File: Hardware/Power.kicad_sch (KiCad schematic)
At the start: 12 parts

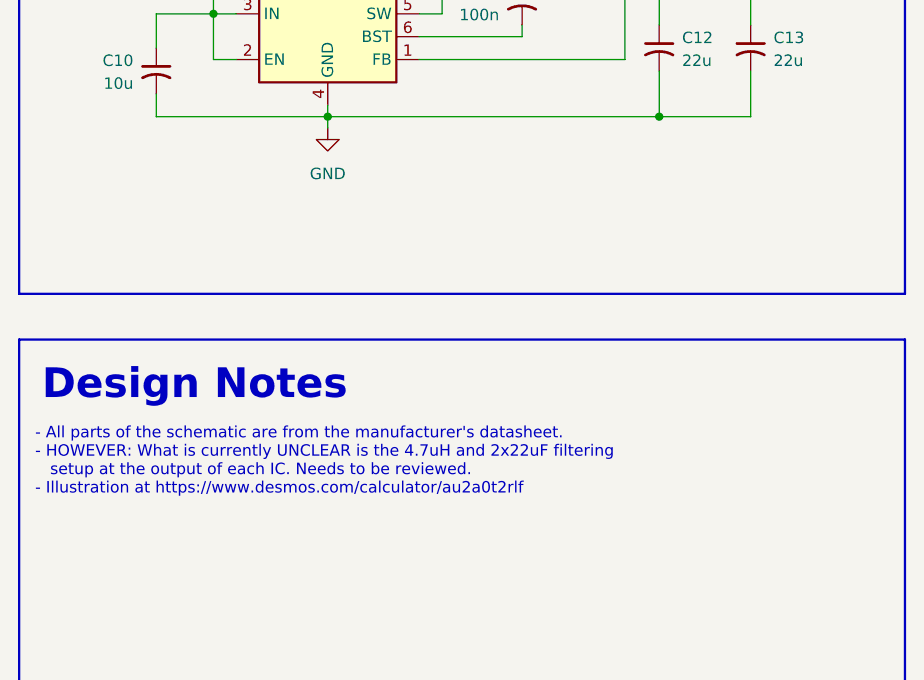
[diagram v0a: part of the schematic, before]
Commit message: Finished the ISOW1044 Schematic
- Ported over Kostadin's schematic

Co-authored-by: Kostadin Madjovski <155325994+bivein@users.noreply.github.com>
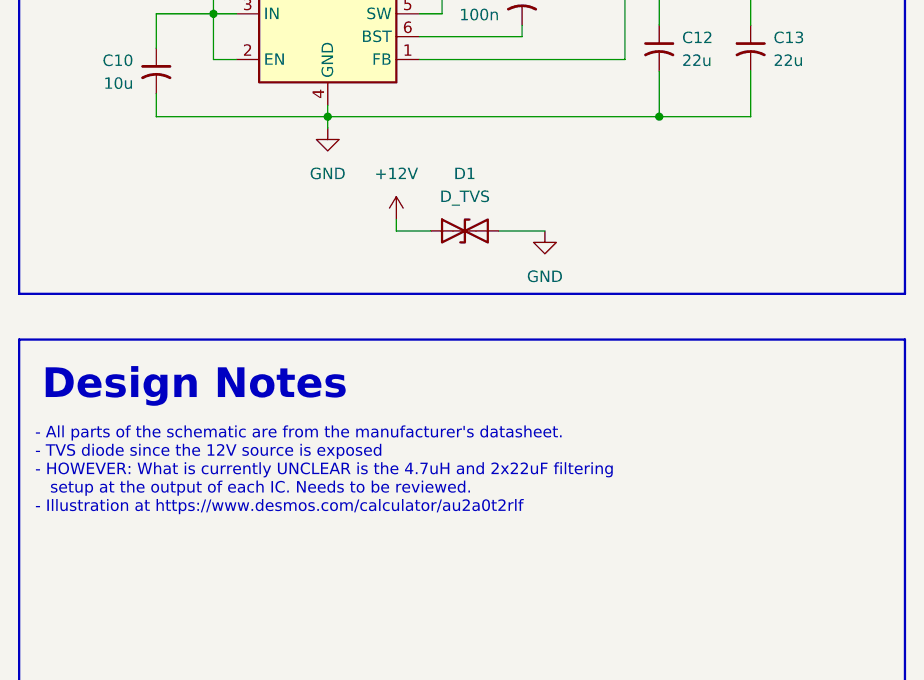
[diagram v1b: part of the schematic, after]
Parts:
- added D1: D_TVS, symbol Device:D_TVS
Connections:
- net +12V: now also D1.1 (A1)
- net GND: now also D1.2 (A2)
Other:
- note added: "- All parts of the schematic are from the manufacturer's datasheet. - TVS diode since the 12V source is exposed - HOWEVER: What is currently UNCLEAR is the 4.7uH and 2x22uF filtering setup at the output of each IC. Needs to be reviewed. - Illustration at https://www.desmos.com/calculator/au2a0t2rlf"
- note removed: "- All parts of the schematic are from the manufacturer's datasheet. - HOWEVER: What is currently UNCLEAR is the 4.7uH and 2x22uF filtering setup at the output of each IC. Needs to be reviewed. - Illustration at https://www.desmos.com/calculator/au2a0t2rlf"
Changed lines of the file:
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@@
 		)
 	)
-	(text "- All parts of the schematic are from the manufacturer's datasheet.\n- HOWEVER: What is currently UNCLEAR is the 4.7uH and 2x22uF filtering\n   setup at the output of each IC. Needs to be reviewed.\n- Illustration at https://www.desmos.com/calculator/au2a0t2rlf"
+	(text "- All parts of the schematic are from the manufacturer's datasheet.\n- TVS diode since the 12V source is exposed\n- HOWEVER: What is currently UNCLEAR is the 4.7uH and 2x22uF filtering\n   setup at the output of each IC. Needs to be reviewed.\n- Illustration at https://www.desmos.com/calculator/au2a0t2rlf"
 		(exclude_from_sim no)
 		(at 17.018 124.714 0)
@@
 	(wire
 		(pts
+			(xy 68.58 102.87) (xy 73.66 102.87)
+		)
+		(stroke
+			(width 0)
+			(type default)
+		)
+	)
+	(wire
+		(pts
 			(xy 96.52 73.66) (xy 86.36 73.66)
 		)
@@
 	(wire
 		(pts
+			(xy 57.15 102.87) (xy 57.15 101.6)
+		)
+		(stroke
+			(width 0)
+			(type default)
+		)
+	)
+	(wire
+		(pts
 			(xy 86.36 73.66) (xy 86.36 80.01)
 		)
@@
 		(pts
 			(xy 96.52 44.45) (xy 96.52 38.1)
+		)
+		(stroke
+			(width 0)
+			(type default)
+		)
+	)
+	(wire
+		(pts
+			(xy 60.96 102.87) (xy 57.15 102.87)
 		)
 		(stroke
@@
 	)
 	(symbol
+		(lib_id "power:+12V")
+		(at 57.15 101.6 0)
+		(unit 1)
+		(exclude_from_sim no)
+		(in_bom yes)
+		(on_board yes)
+		(dnp no)
+		(fields_autoplaced yes)
+		(property "Reference" "#PWR011"
+			(at 57.15 105.41 0)
+			(effects
+				(font
+					(size 1.27 1.27)
+				)
+				(hide yes)
+			)
+		)
+		(property "Value" "+12V"
+			(at 57.15 96.52 0)
+			(effects
+				(font
+					(size 1.27 1.27)
+				)
+			)
+		)
+		(property "Footprint" ""
+			(at 57.15 101.6 0)
+			(effects
+				(font
+					(size 1.27 1.27)
+				)
+				(hide yes)
+			)
+		)
+		(property "Datasheet" ""
+			(at 57.15 101.6 0)
+			(effects
+				(font
+					(size 1.27 1.27)
+				)
+				(hide yes)
+			)
+		)
+		(property "Description" "Power symbol creates a global label with name \"+12V\""
+			(at 57.15 101.6 0)
+			(effects
+				(font
+					(size 1.27 1.27)
+				)
+				(hide yes)
+			)
+		)
+		(pin "1"
+		)
+		(instances
+			(project "CANIO-Board"
+				(path "/a11f98b2-3b09-4cf9-8535-19e509fe91b9/689b7a23-36b5-40a7-9bc7-70c150316ec6"
+					(reference "#PWR011")
+					(unit 1)
+				)
+			)
+		)
+	)
+	(symbol
 		(lib_id "power:PWR_FLAG")
 		(at 96.52 38.1 0)
@@
 	)
 	(symbol
+		(lib_id "power:GND")
+		(at 73.66 102.87 0)
+		(unit 1)
+		(exclude_from_sim no)
+		(in_bom yes)
+		(on_board yes)
+		(dnp no)
+		(fields_autoplaced yes)
+		(property "Reference" "#PWR012"
+			(at 73.66 109.22 0)
+			(effects
+				(font
+					(size 1.27 1.27)
+				)
+				(hide yes)
+			)
+		)
+		(property "Value" "GND"
+			(at 73.66 107.95 0)
+			(effects
+				(font
+					(size 1.27 1.27)
+				)
+			)
+		)
+		(property "Footprint" ""
+			(at 73.66 102.87 0)
+			(effects
+				(font
+					(size 1.27 1.27)
+				)
+				(hide yes)
+			)
+		)
+		(property "Datasheet" ""
+			(at 73.66 102.87 0)
+			(effects
+				(font
+					(size 1.27 1.27)
+				)
+				(hide yes)
+			)
+		)
+		(property "Description" "Power symbol creates a global label with name \"GND\" , ground"
+			(at 73.66 102.87 0)
+			(effects
+				(font
+					(size 1.27 1.27)
+				)
+				(hide yes)
+			)
+		)
+		(pin "1"
+		)
+		(instances
+			(project "CANIO-Board"
+				(path "/a11f98b2-3b09-4cf9-8535-19e509fe91b9/689b7a23-36b5-40a7-9bc7-70c150316ec6"
+					(reference "#PWR012")
+					(unit 1)
+				)
+			)
+		)
+	)
+	(symbol
 		(lib_id "Device:C_Small_US")
 		(at 71.12 41.91 0)
@@
 					(unit 1)
 				)
+			)
+		)
+	)
+	(symbol
+		(lib_id "Device:D_TVS")
+		(at 64.77 102.87 0)
+		(unit 1)
+		(exclude_from_sim no)
+		(in_bom yes)
+		(on_board yes)
+		(dnp no)
+		(fields_autoplaced yes)
+		(property "Reference" "D1"
+			(at 64.77 96.52 0)
+			(effects
+				(font
+					(size 1.27 1.27)
+				)
+			)
+		)
+		(property "Value" "D_TVS"
+			(at 64.77 99.06 0)
+			(effects
+				(font
+					(size 1.27 1.27)
+				)
+			)
+		)
+		(property "Footprint" ""
+			(at 64.77 102.87 0)
+			(effects
+				(font
+					(size 1.27 1.27)
+				)
+				(hide yes)
+			)
+		)
+		(property "Datasheet" "~"
+			(at 64.77 102.87 0)
+			(effects
+				(font
+					(size 1.27 1.27)
+				)
+				(hide yes)
+			)
+		)
+		(property "Description" "Bidirectional transient-voltage-suppression diode"
+			(at 64.77 102.87 0)
+			(effects
+				(font
+					(size 1.27 1.27)
+				)
+				(hide yes)
+			)
+		)
+		(pin "2"
+		)
+		(pin "1"
+		)
+		(instances
+			(project ""
+				(path "/a11f98b2-3b09-4cf9-8535-19e509fe91b9/689b7a23-36b5-40a7-9bc7-70c150316ec6"
+					(reference "D1")
+					(unit 1)
+				)

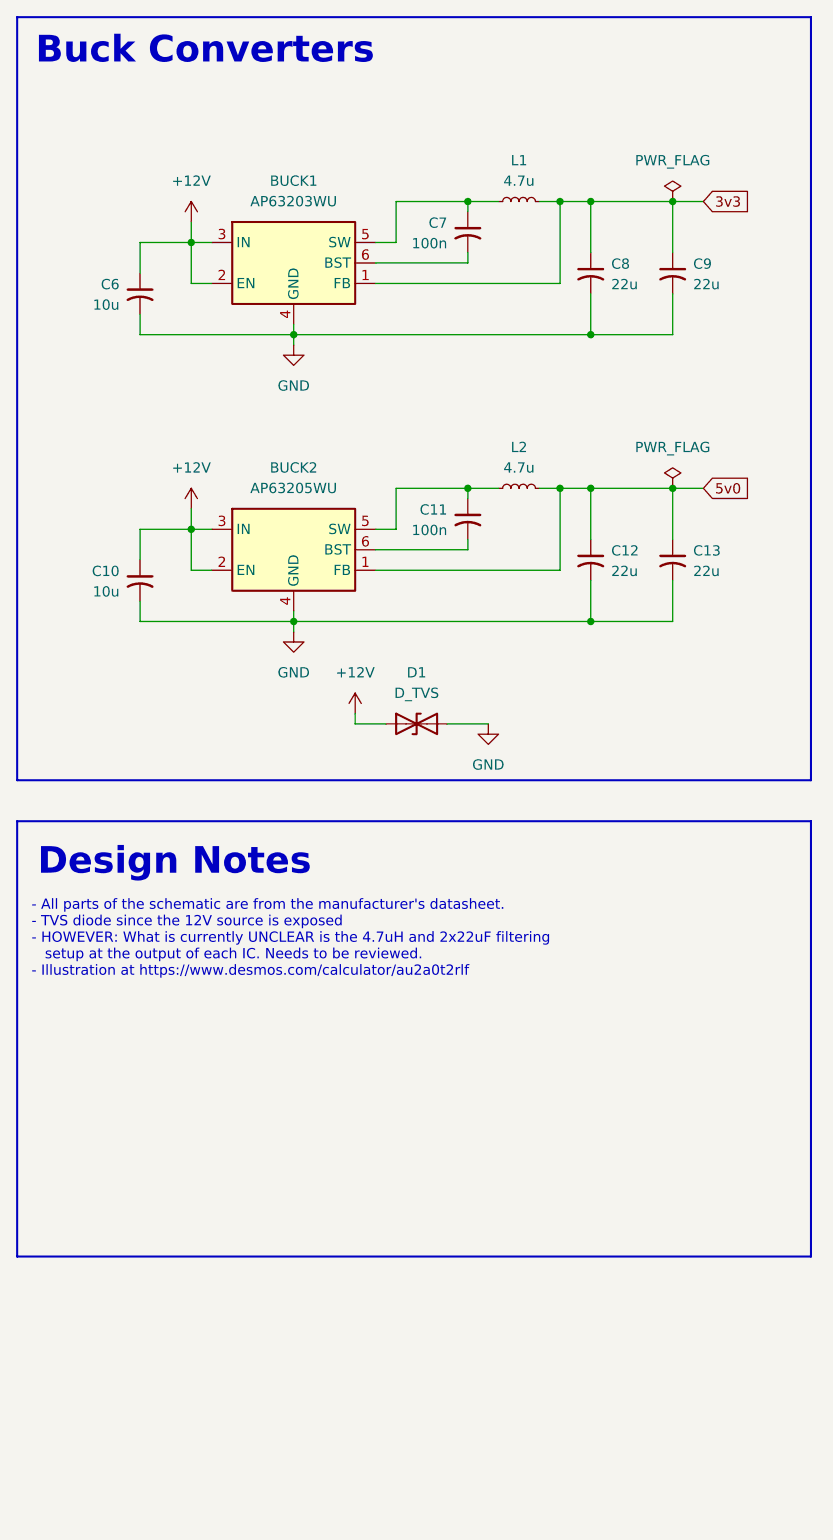
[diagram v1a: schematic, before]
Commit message: Finished final touches on schematic.
- Schematic is complete (NOT yet checked by Yassa/Val)
- ERC check is complete, understandable errors excused w/ comments
- Final schematic formatting complete

Co-authored-by: Kostadin Madjovski <155325994+bivein@users.noreply.github.com>
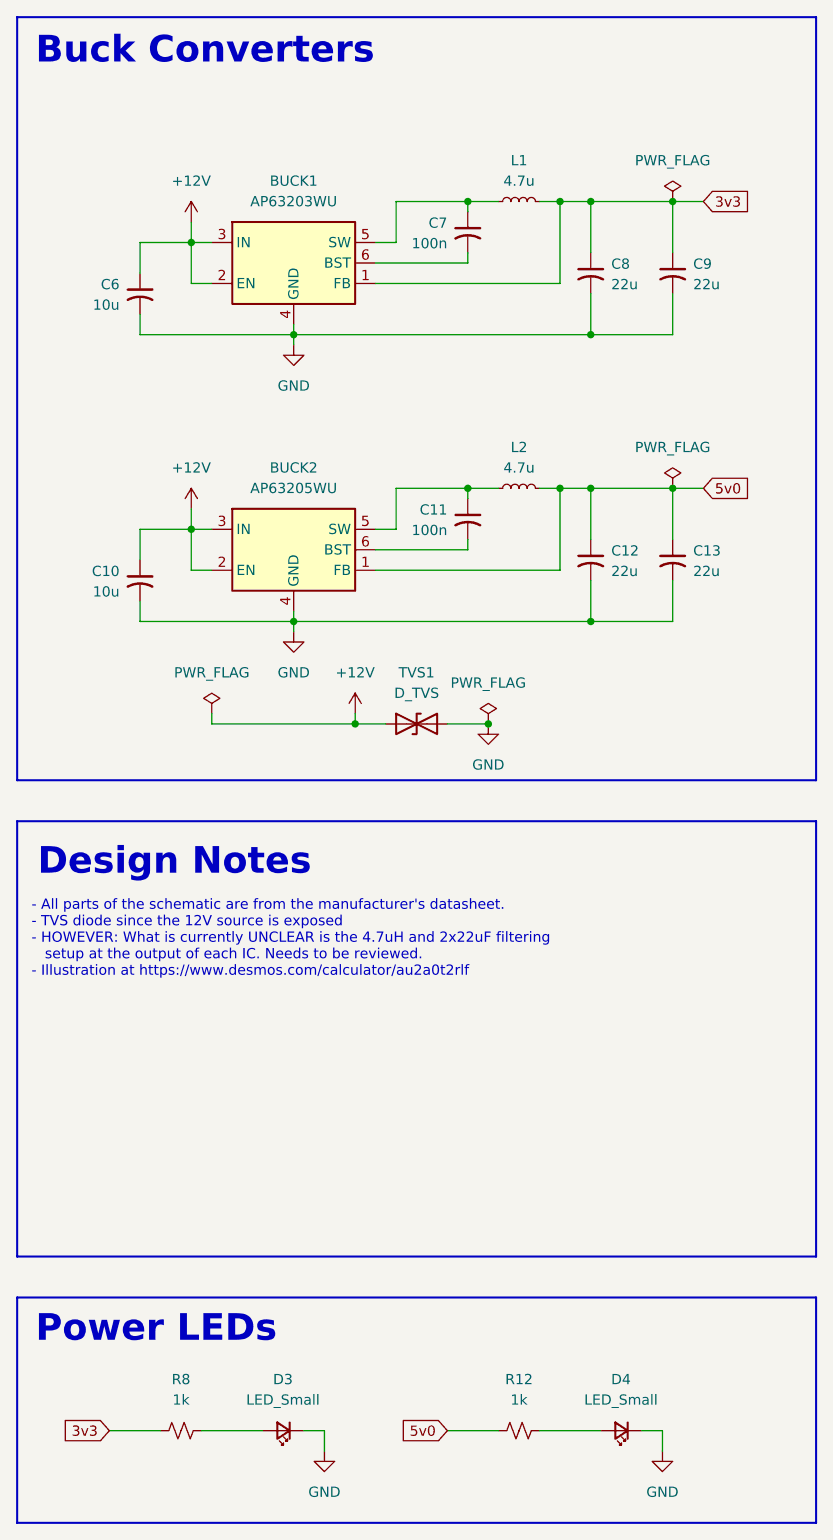
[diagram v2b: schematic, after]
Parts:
- added D3, D4: LED_Small, symbol Device:LED_Small
- added R12, R8: 1k, symbol Device:R_Small_US
- renumbered D1 to TVS1
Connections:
- net 3v3: now also R8.1
- net 5v0: now also R12.1
- net GND: now also D3.1 (K), D4.1 (K)
- new net: D4.2 (A), R12.2
- new net: D3.2 (A), R8.2
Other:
- note added: "Power LEDs"
- company: (none) -> NJIT Solar Car
- title: (none) -> CAN IO Board | Power
